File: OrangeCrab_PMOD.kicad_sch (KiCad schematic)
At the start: 1 part

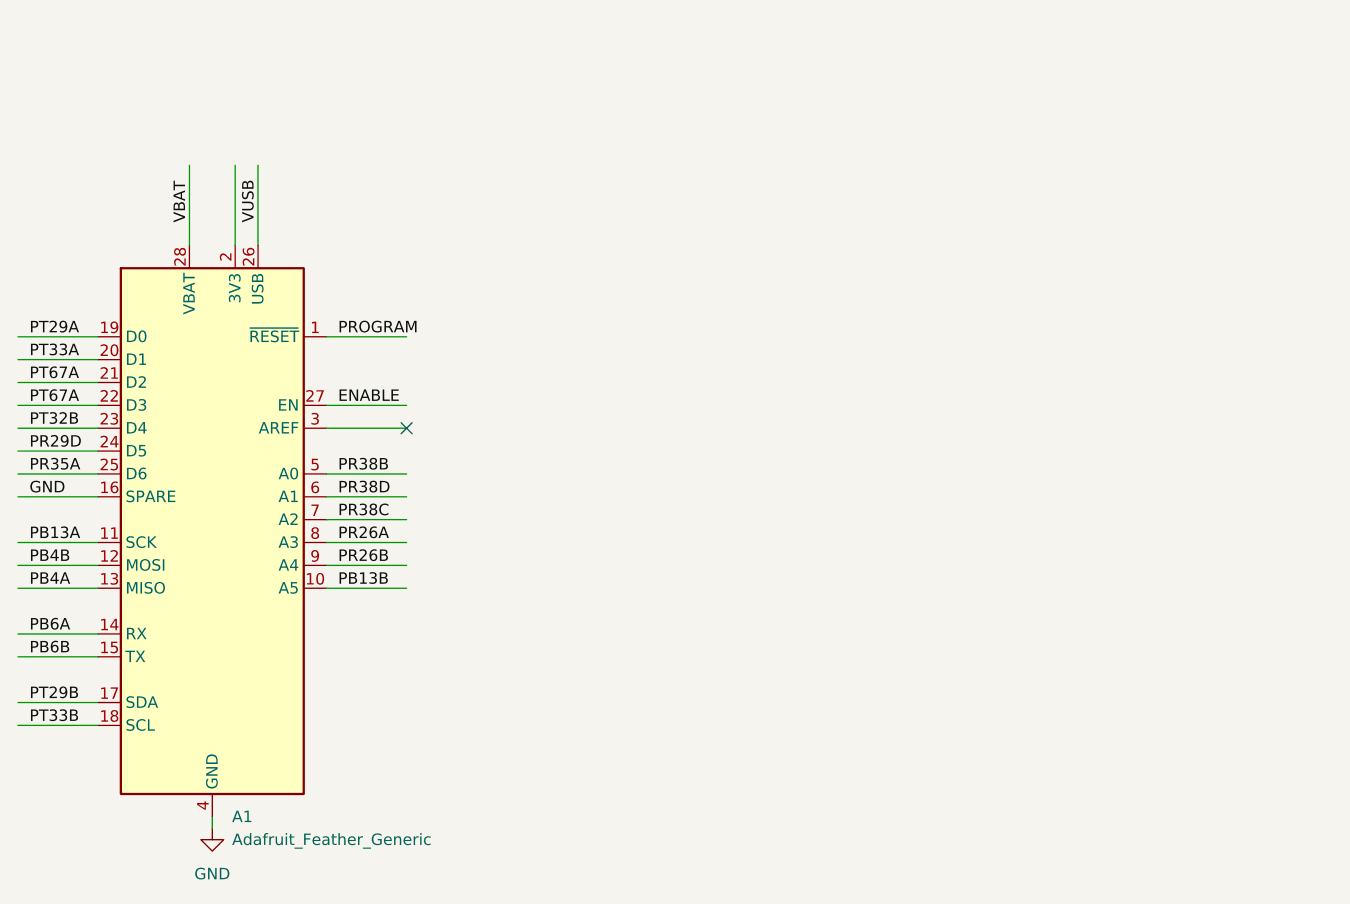
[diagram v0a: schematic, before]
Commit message: started layout and connectors to Orange Crab
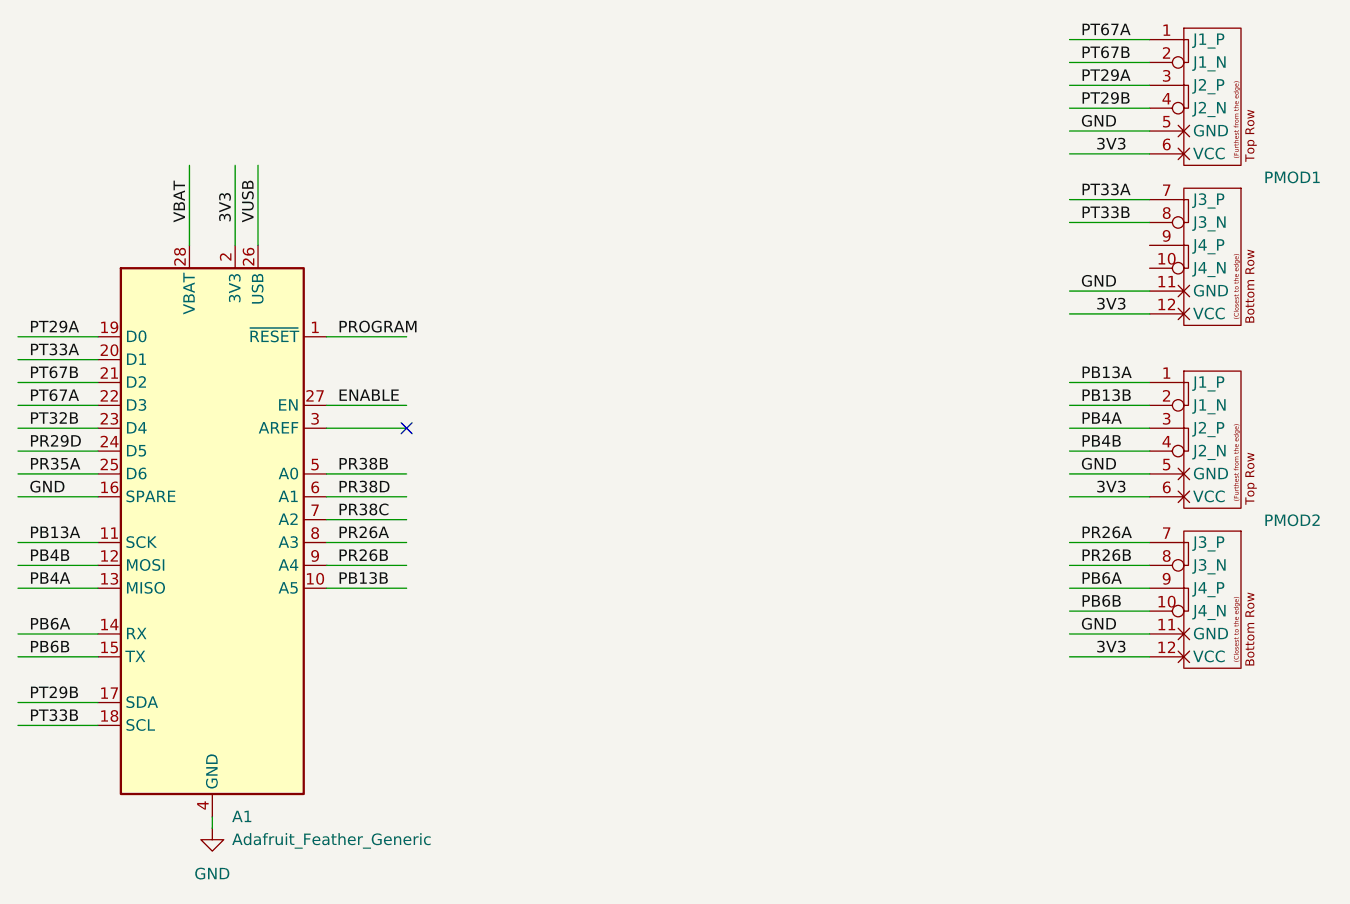
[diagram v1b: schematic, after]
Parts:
- added PMOD1, PMOD2: PMOD-Device-x2-Type-XHS, pmod-conn_6x2:pmod_pin_array_6x2, symbol pmod:PMOD-Device-x2-Type-XHS
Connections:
- net GND: now also PMOD1.11 (GND), PMOD1.5 (GND), PMOD2.11 (GND), PMOD2.5 (GND)
- net PB13A: now also PMOD2.1 (J1_P)
- net PB13B: now also PMOD2.2 (J1_N)
- net PB4A: now also PMOD2.3 (J2_P)
- net PB4B: now also PMOD2.4 (J2_N)
- net PB6A: now also PMOD2.9 (J4_P)
- net PB6B: now also PMOD2.10 (J4_N)
- net PR26A: now also PMOD2.7 (J3_P)
- net PR26B: now also PMOD2.8 (J3_N)
- net PT29A: now also PMOD1.3 (J2_P)
- net PT29B: now also PMOD1.4 (J2_N)
- net PT33A: now also PMOD1.7 (J3_P)
- net PT33B: now also PMOD1.8 (J3_N)
- net PT67A: now also PMOD1.1 (J1_P); no longer A1.21 (D2)
- net 3V3: now reaches A1.2 (3V3)
- net 3V3: now also PMOD1.12 (VCC), PMOD1.6 (VCC), PMOD2.12 (VCC), PMOD2.6 (VCC)
- new net PT67B: A1.21 (D2), PMOD1.2 (J1_N)
